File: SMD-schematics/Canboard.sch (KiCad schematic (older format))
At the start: 12 parts, among them J1 Barrel_Jack, J2 Screw_Terminal_01x02, J3 USB_OTG, J4 Conn_Debug, U1 L7805

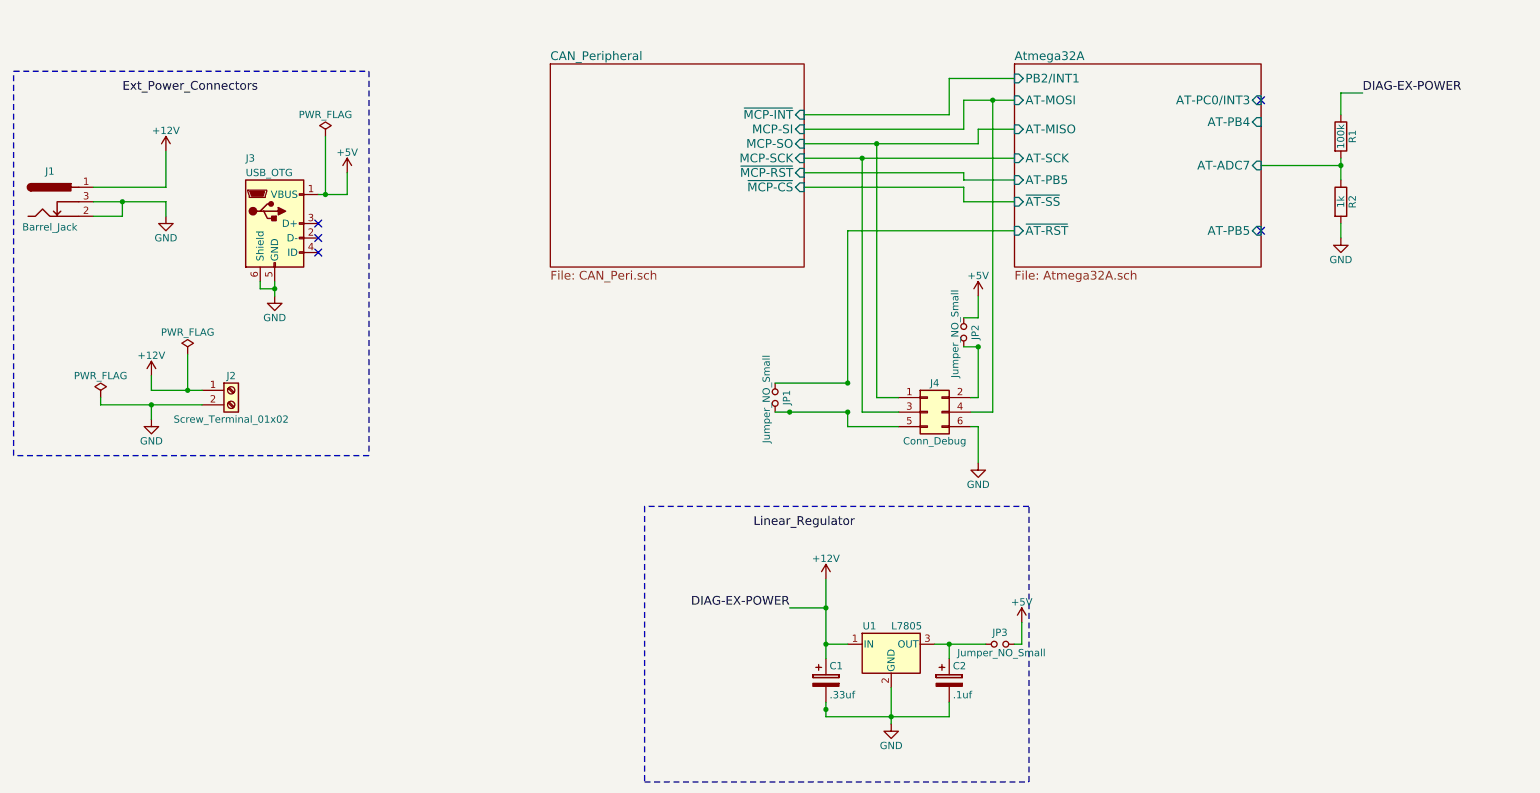
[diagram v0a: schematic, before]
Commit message: Adding DebugWIRE and modifications on ISP, UART, SPI connections
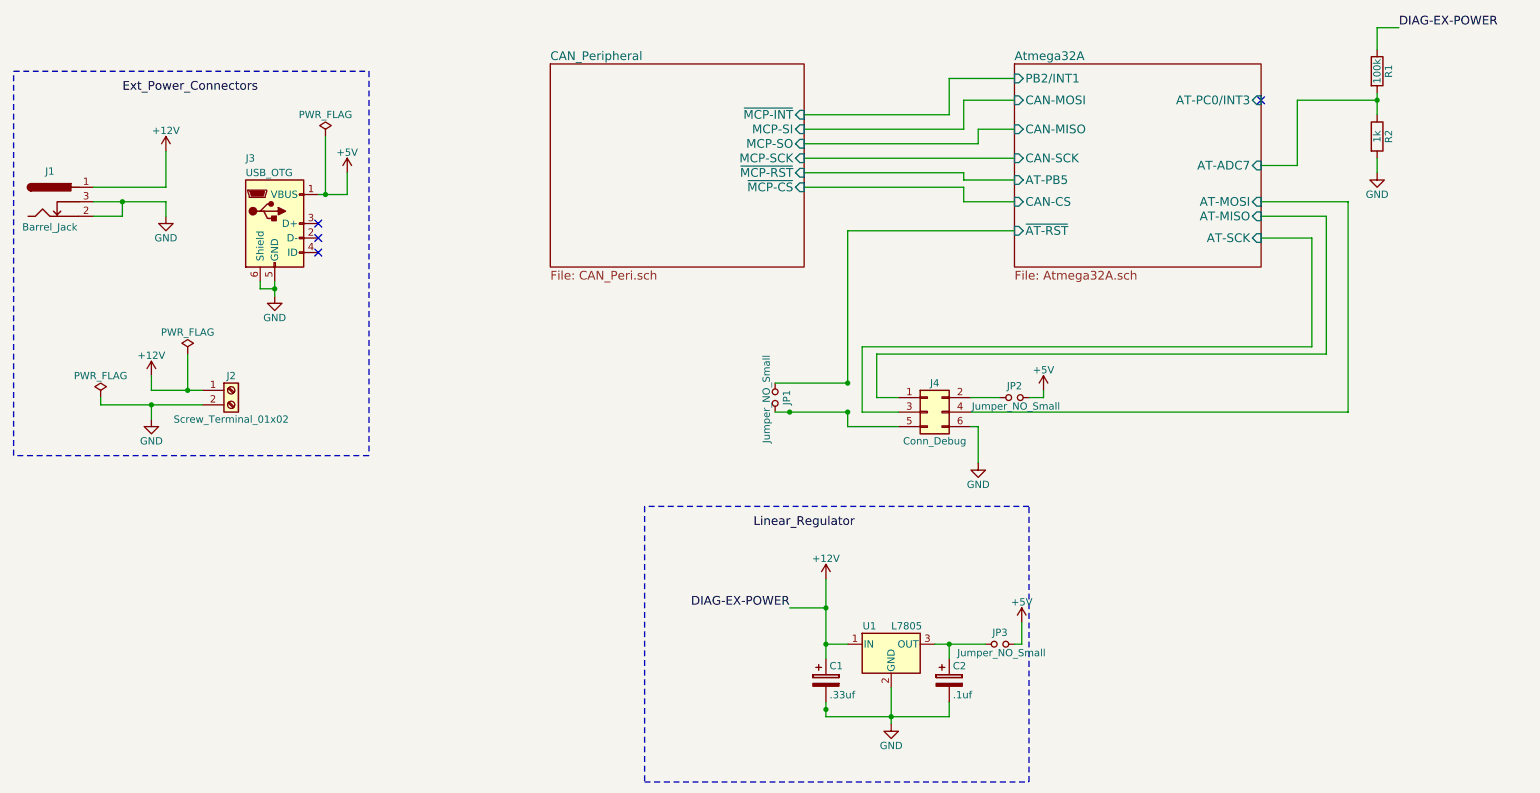
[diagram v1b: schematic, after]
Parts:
- J4: footprint Pin_Headers:Pin_Header_Straight_2x03_Pitch2.54mm -> Pin_Headers:Pin_Header_Straight_2x03_Pitch2.54mm_SMD
- JP1, JP2, JP3: footprint Pin_Headers:Pin_Header_Straight_1x02_Pitch2.54mm -> Pin_Headers:Pin_Header_Straight_1x02_Pitch2.54mm_SMD_Pin1Left
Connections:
- net +5V: now also JP2.2; no longer JP2.1
- net at J4.2 (Pin_2): now also JP2.1; no longer JP2.2
- no-connect marks 5 -> 4
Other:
- moved on the sheet: JP2, R1, R2
